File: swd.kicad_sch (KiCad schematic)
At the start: 7 parts, among them J12 Conn_ARM_JTAG_SWD_10, U13 RCLAMP0504F.TCT

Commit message: feat: add board dimensions and change mcu position
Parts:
- renumbered TP26 to TP22, TP27 to TP23, TP28 to TP24, TP29 to TP25
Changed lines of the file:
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@@
 		(in_pos_files yes)
 		(dnp no)
-		(property "Reference" "TP29"
+		(property "Reference" "TP25"
 			(at 217.17 79.5021 0)
 			(show_name no)
@@
 			(project "reflow_station"
 				(path "/77770e37-dda2-4cf3-b2f1-cea4793bc3be/93249a2a-e51b-4c44-9b6d-4c6bfcead48b/235cb61c-0bfd-4530-98f3-9fb88eaf14c4"
-					(reference "TP29")
+					(reference "TP25")
 					(unit 1)
 				)
@@
 		(in_pos_files yes)
 		(dnp no)
-		(property "Reference" "TP28"
+		(property "Reference" "TP24"
 			(at 219.71 73.1521 0)
 			(show_name no)
@@
 			(project "reflow_station"
 				(path "/77770e37-dda2-4cf3-b2f1-cea4793bc3be/93249a2a-e51b-4c44-9b6d-4c6bfcead48b/235cb61c-0bfd-4530-98f3-9fb88eaf14c4"
-					(reference "TP28")
+					(reference "TP24")
 					(unit 1)
 				)
@@
 		(in_pos_files yes)
 		(dnp no)
-		(property "Reference" "TP26"
+		(property "Reference" "TP22"
 			(at 217.17 44.9579 0)
 			(show_name no)
@@
 			(project "reflow_station"
 				(path "/77770e37-dda2-4cf3-b2f1-cea4793bc3be/93249a2a-e51b-4c44-9b6d-4c6bfcead48b/235cb61c-0bfd-4530-98f3-9fb88eaf14c4"
-					(reference "TP26")
+					(reference "TP22")
 					(unit 1)
 				)
@@
 		(in_pos_files yes)
 		(dnp no)
-		(property "Reference" "TP27"
+		(property "Reference" "TP23"
 			(at 219.71 51.3079 0)
 			(show_name no)
@@
 			(project "reflow_station"
 				(path "/77770e37-dda2-4cf3-b2f1-cea4793bc3be/93249a2a-e51b-4c44-9b6d-4c6bfcead48b/235cb61c-0bfd-4530-98f3-9fb88eaf14c4"
-					(reference "TP27")
+					(reference "TP23")
 					(unit 1)
 				)

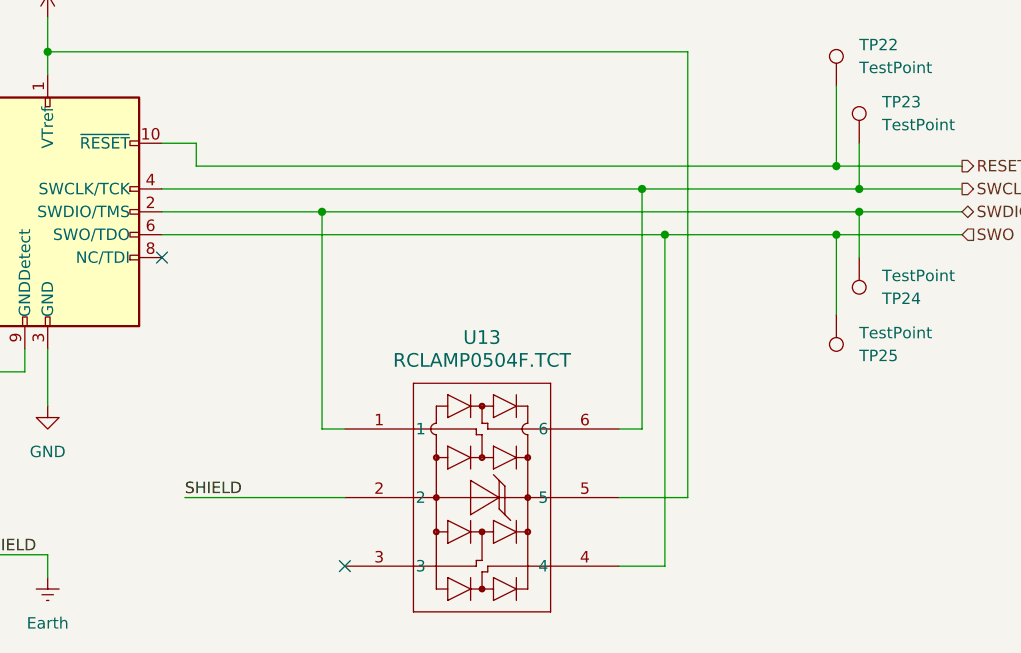
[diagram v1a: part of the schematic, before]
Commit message: feat: route config switches and SWD debug
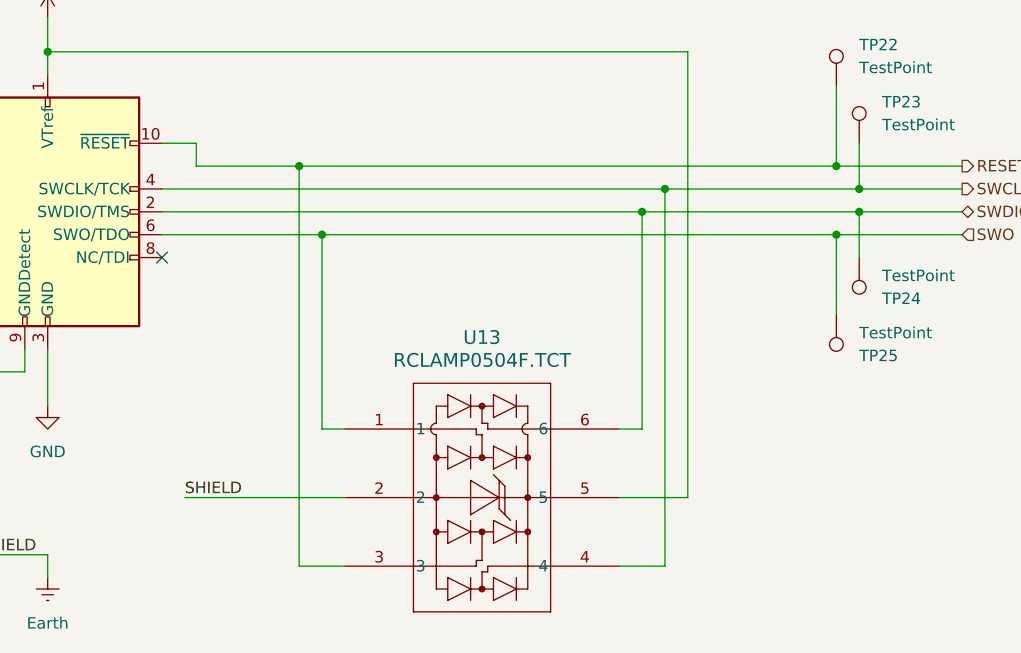
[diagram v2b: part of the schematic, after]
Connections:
- net RESET#: now also U13.3
- net SWCLK: now also U13.4; no longer U13.6
- net SWDIO: now also U13.6; no longer U13.1
- net SWO: now also U13.1; no longer U13.4
- no-connect marks 2 -> 1
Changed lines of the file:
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@@
+	)
+	(junction
+		(at 154.94 58.42)
+		(diameter 0)
+		(color 0 0 0 0)
 	)
 	(junction
@@
 	)
 	(junction
-		(at 193.04 60.96)
-		(diameter 0)
-		(color 0 0 0 0)
-	)
-	(junction
 		(at 214.63 66.04)
 		(diameter 0)
@@
 	)
 	(junction
-		(at 195.58 66.04)
-		(diameter 0)
-		(color 0 0 0 0)
-	)
-	(junction
 		(at 214.63 58.42)
 		(diameter 0)
@@
 	)
 	(junction
-		(at 157.48 63.5)
-		(diameter 0)
-		(color 0 0 0 0)
-	)
-	(no_connect
-		(at 160.02 102.87)
+		(at 195.58 60.96)
+		(diameter 0)
+		(color 0 0 0 0)
+	)
+	(junction
+		(at 157.48 66.04)
+		(diameter 0)
+		(color 0 0 0 0)
+	)
+	(junction
+		(at 193.04 63.5)
+		(diameter 0)
+		(color 0 0 0 0)
 	)
 	(no_connect
@@
 	(wire
 		(pts
-			(xy 157.48 63.5) (xy 217.17 63.5)
-		)
-		(stroke
-			(width 0)
-			(type default)
-		)
-	)
-	(wire
-		(pts
 			(xy 104.14 101.6) (xy 104.14 104.14)
 		)
@@
 	(wire
 		(pts
+			(xy 193.04 63.5) (xy 193.04 87.63)
+		)
+		(stroke
+			(width 0)
+			(type default)
+		)
+	)
+	(wire
+		(pts
+			(xy 195.58 60.96) (xy 217.17 60.96)
+		)
+		(stroke
+			(width 0)
+			(type default)
+		)
+	)
+	(wire
+		(pts
 			(xy 160.02 87.63) (xy 157.48 87.63)
 		)
@@
 	(wire
 		(pts
-			(xy 143.51 58.42) (xy 214.63 58.42)
+			(xy 143.51 58.42) (xy 154.94 58.42)
 		)
 		(stroke
@@
 	(wire
 		(pts
+			(xy 160.02 102.87) (xy 154.94 102.87)
+		)
+		(stroke
+			(width 0)
+			(type default)
+		)
+	)
+	(wire
+		(pts
+			(xy 157.48 66.04) (xy 214.63 66.04)
+		)
+		(stroke
+			(width 0)
+			(type default)
+		)
+	)
+	(wire
+		(pts
 			(xy 214.63 58.42) (xy 228.6 58.42)
 		)
@@
 	(wire
 		(pts
+			(xy 193.04 63.5) (xy 217.17 63.5)
+		)
+		(stroke
+			(width 0)
+			(type default)
+		)
+	)
+	(wire
+		(pts
 			(xy 114.3 101.6) (xy 127 101.6)
 		)
@@
 	(wire
 		(pts
-			(xy 157.48 87.63) (xy 157.48 63.5)
+			(xy 195.58 60.96) (xy 195.58 102.87)
 		)
 		(stroke
@@
 	(wire
 		(pts
+			(xy 154.94 58.42) (xy 214.63 58.42)
+		)
+		(stroke
+			(width 0)
+			(type default)
+		)
+	)
+	(wire
+		(pts
 			(xy 217.17 55.88) (xy 217.17 60.96)
 		)
@@
 	(wire
 		(pts
-			(xy 193.04 60.96) (xy 217.17 60.96)
-		)
-		(stroke
-			(width 0)
-			(type default)
-		)
-	)
-	(wire
-		(pts
 			(xy 127 104.14) (xy 127 101.6)
 		)
@@
 	(wire
 		(pts
-			(xy 139.7 60.96) (xy 193.04 60.96)
+			(xy 139.7 60.96) (xy 195.58 60.96)
+		)
+		(stroke
+			(width 0)
+			(type default)
+		)
+	)
+	(wire
+		(pts
+			(xy 157.48 87.63) (xy 157.48 66.04)
 		)
 		(stroke
@@
 	(wire
 		(pts
-			(xy 139.7 63.5) (xy 157.48 63.5)
-		)
-		(stroke
-			(width 0)
-			(type default)
-		)
-	)
-	(wire
-		(pts
-			(xy 195.58 102.87) (xy 195.58 66.04)
+			(xy 139.7 63.5) (xy 193.04 63.5)
 		)
 		(stroke
@@
 	(wire
 		(pts
-			(xy 195.58 66.04) (xy 214.63 66.04)
+			(xy 139.7 66.04) (xy 157.48 66.04)
 		)
 		(stroke
@@
 	(wire
 		(pts
-			(xy 139.7 66.04) (xy 195.58 66.04)
-		)
-		(stroke
-			(width 0)
-			(type default)
-		)
-	)
-	(wire
-		(pts
 			(xy 190.5 102.87) (xy 195.58 102.87)
 		)
@@
 	(wire
 		(pts
-			(xy 193.04 87.63) (xy 193.04 60.96)
-		)
-		(stroke
-			(width 0)
-			(type default)
-		)
-	)
-	(wire
-		(pts
 			(xy 124.46 78.74) (xy 124.46 81.28)
 		)
@@
 		)
 		(stroke
+			(width 0)
+			(type default)
+		)
+	)
+	(wire
+		(pts
+			(xy 154.94 58.42) (xy 154.94 102.87)
+		)
+		(stroke
